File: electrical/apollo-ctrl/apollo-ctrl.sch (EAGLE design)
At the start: 62 parts, among them Q1 N-chan, Q2 N-chan, U1 NANO, U2 HONEYWELL-MPR, X1 BARREL-JACK, X2 SENSOR-O2

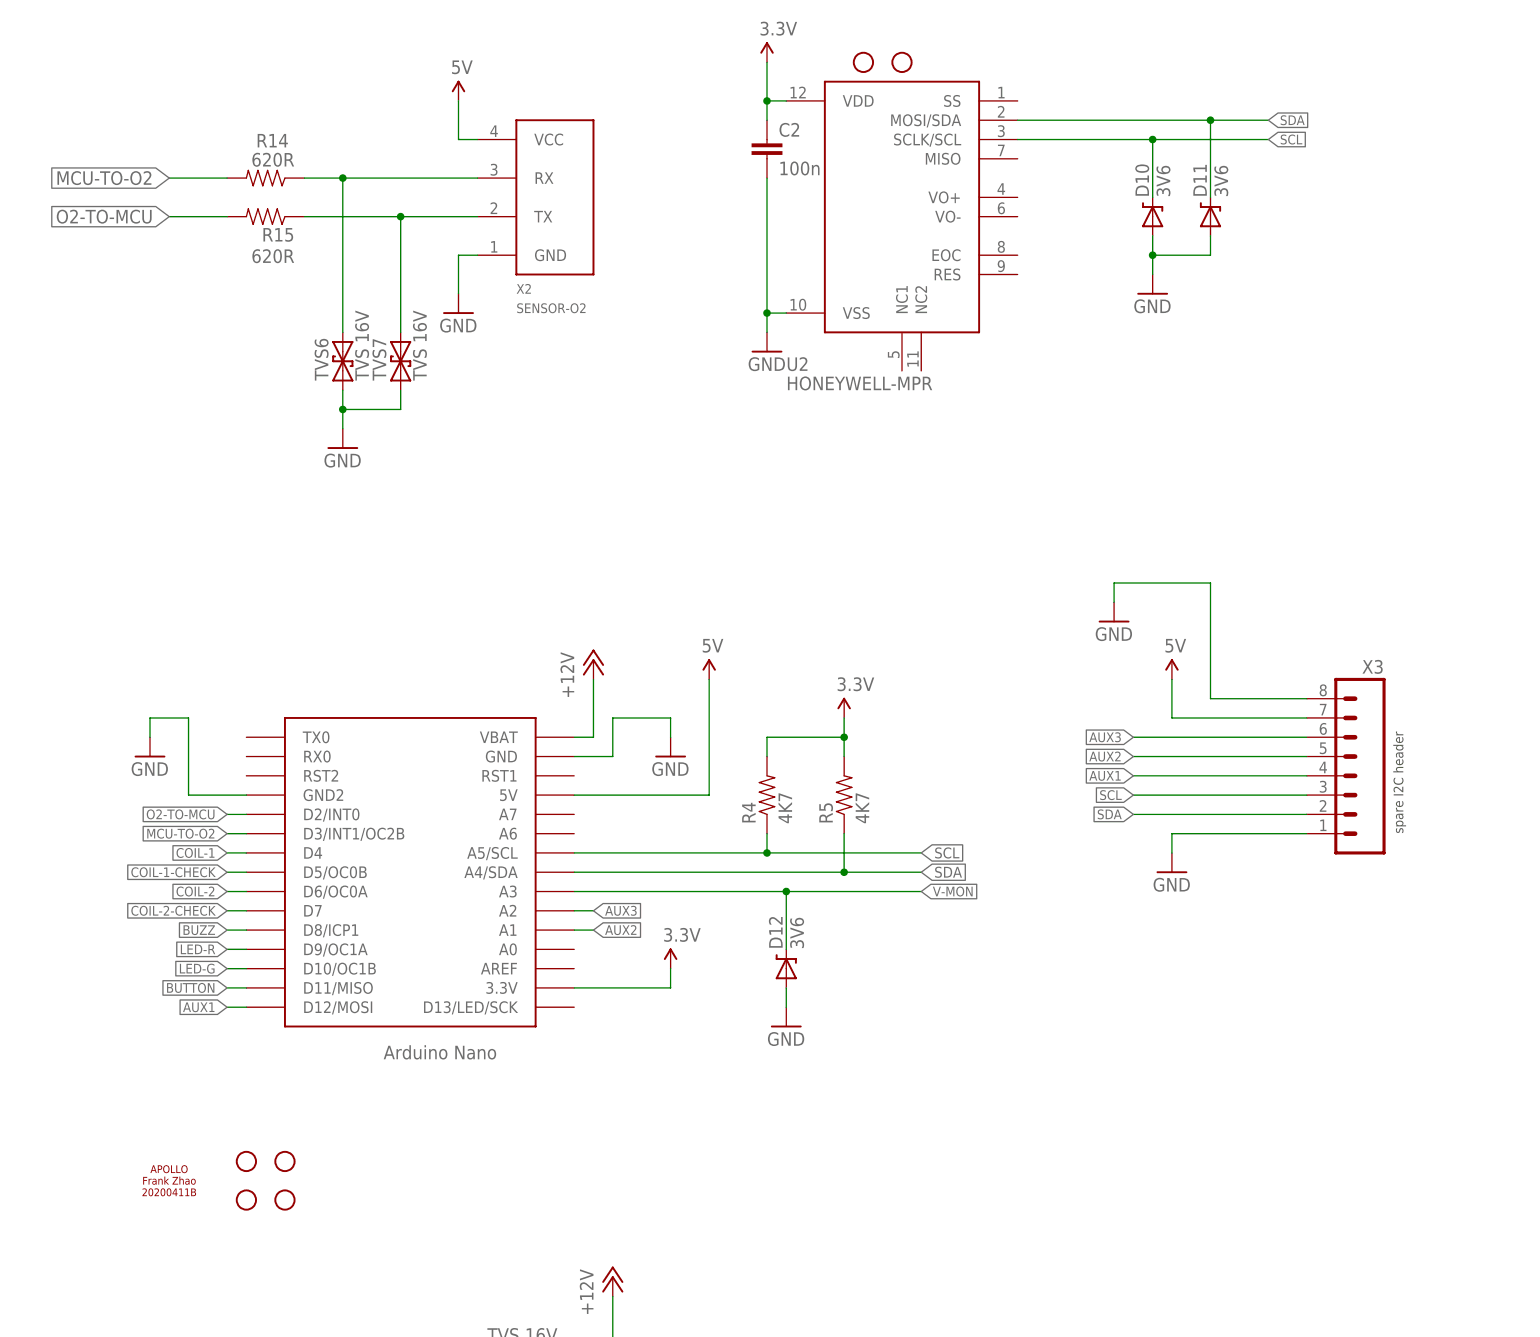
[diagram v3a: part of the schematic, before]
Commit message: changed to use Adafruit MPRLS
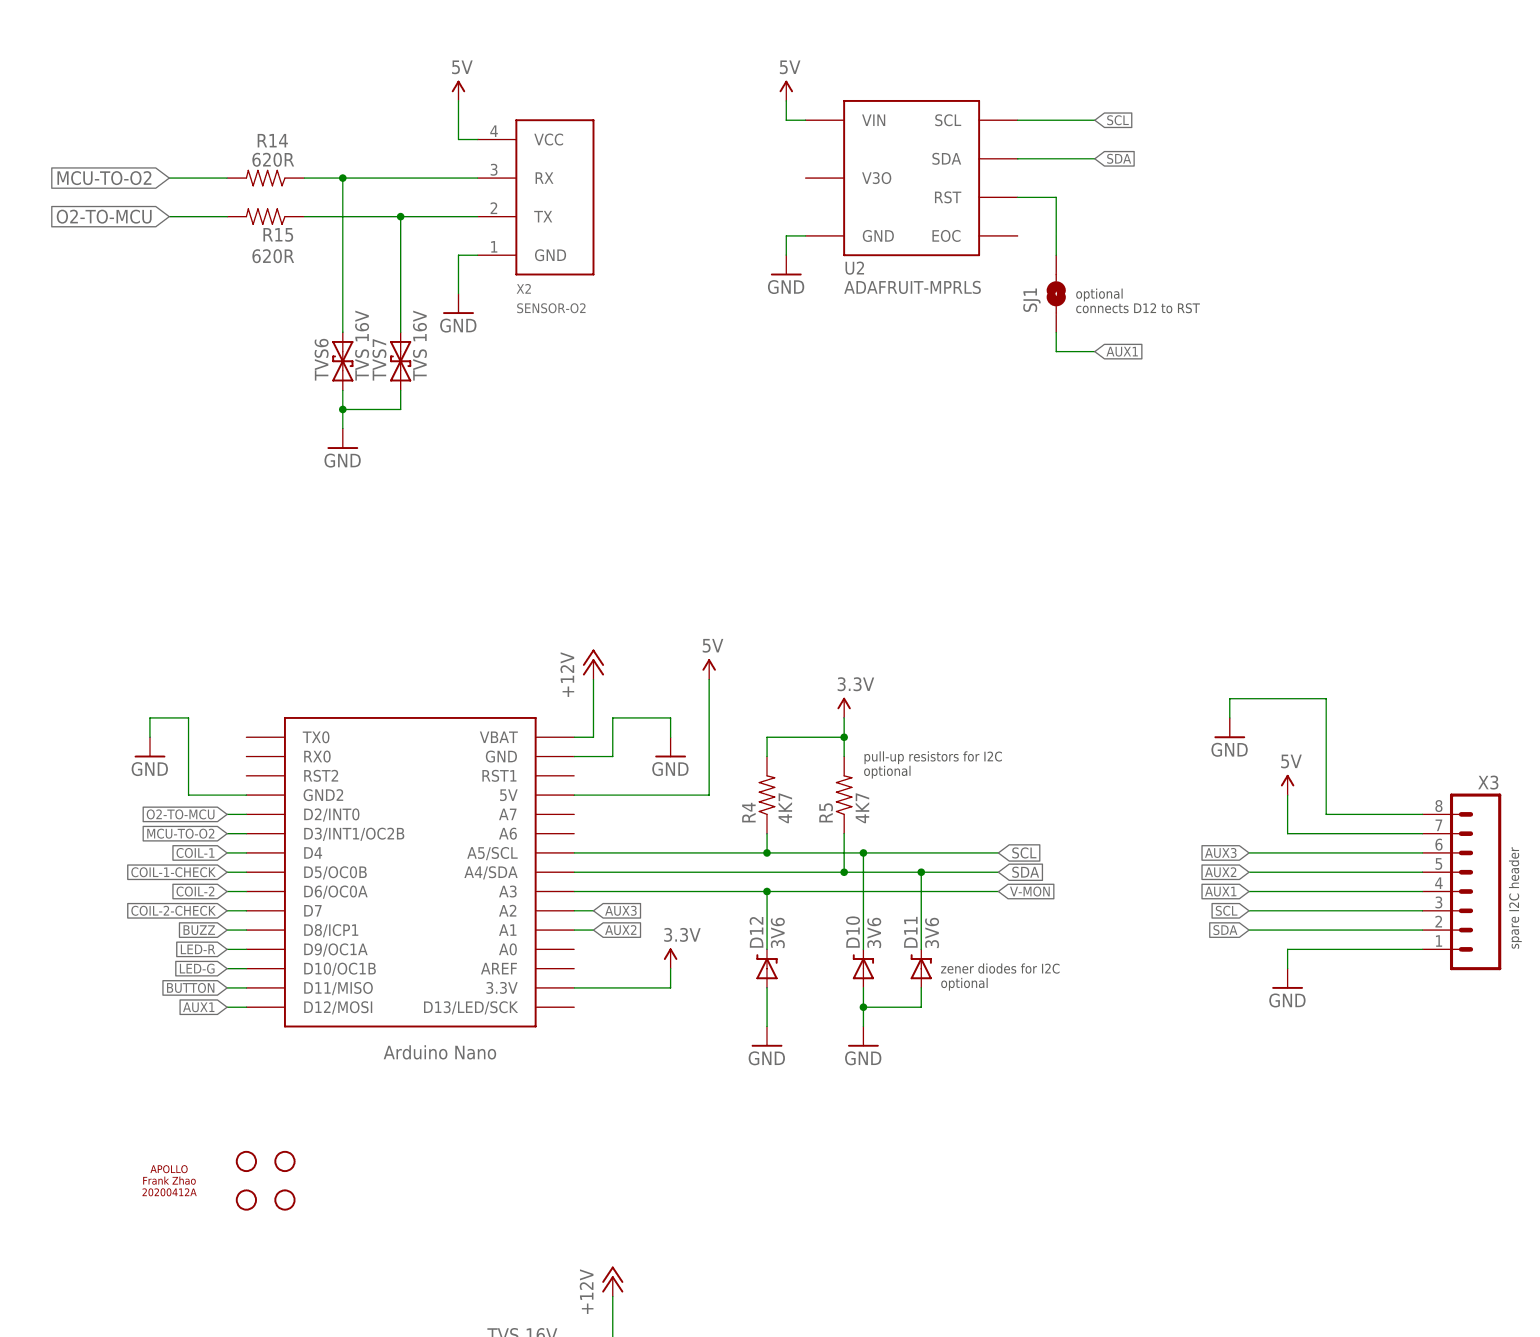
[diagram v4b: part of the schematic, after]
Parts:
- removed C2: 100n, apollo-ctrl:CAPPTH
- removed JP7, JP8: STAND-OFF, apollo-ctrl:STAND-OFF
- added SJ1: SOLDERJUMPERNO, apollo-ctrl:SOLDERJUMPERNO
- U2: value HONEYWELL-MPR -> ADAFRUIT-MPRLS; device apollo-ctrl:HONEYWELL-MPR-GAGE-DIY -> apollo-ctrl:ADAFRUIT-MPRLS-W-HOLES
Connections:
- new net N$1: SJ1.2, U2.RST
- net 3.3V: no longer C2.1, U2.VDD
- net 5V: now also U2.VIN
- net AUX1: now also SJ1.1
- net GND: now also U2.GND; no longer C2.2, U2.VSS
- net SCL: now also U2.SCL; no longer U2.SCLK/SCL
- net SDA: now also U2.SDA; no longer U2.MOSI/SDA
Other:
- note added: "optional connects D12 to RST"
- note added: "pull-up resistors for I2C optional"
- note added: "zener diodes for I2C optional"
- moved on the sheet: D10, D11, D12, X3

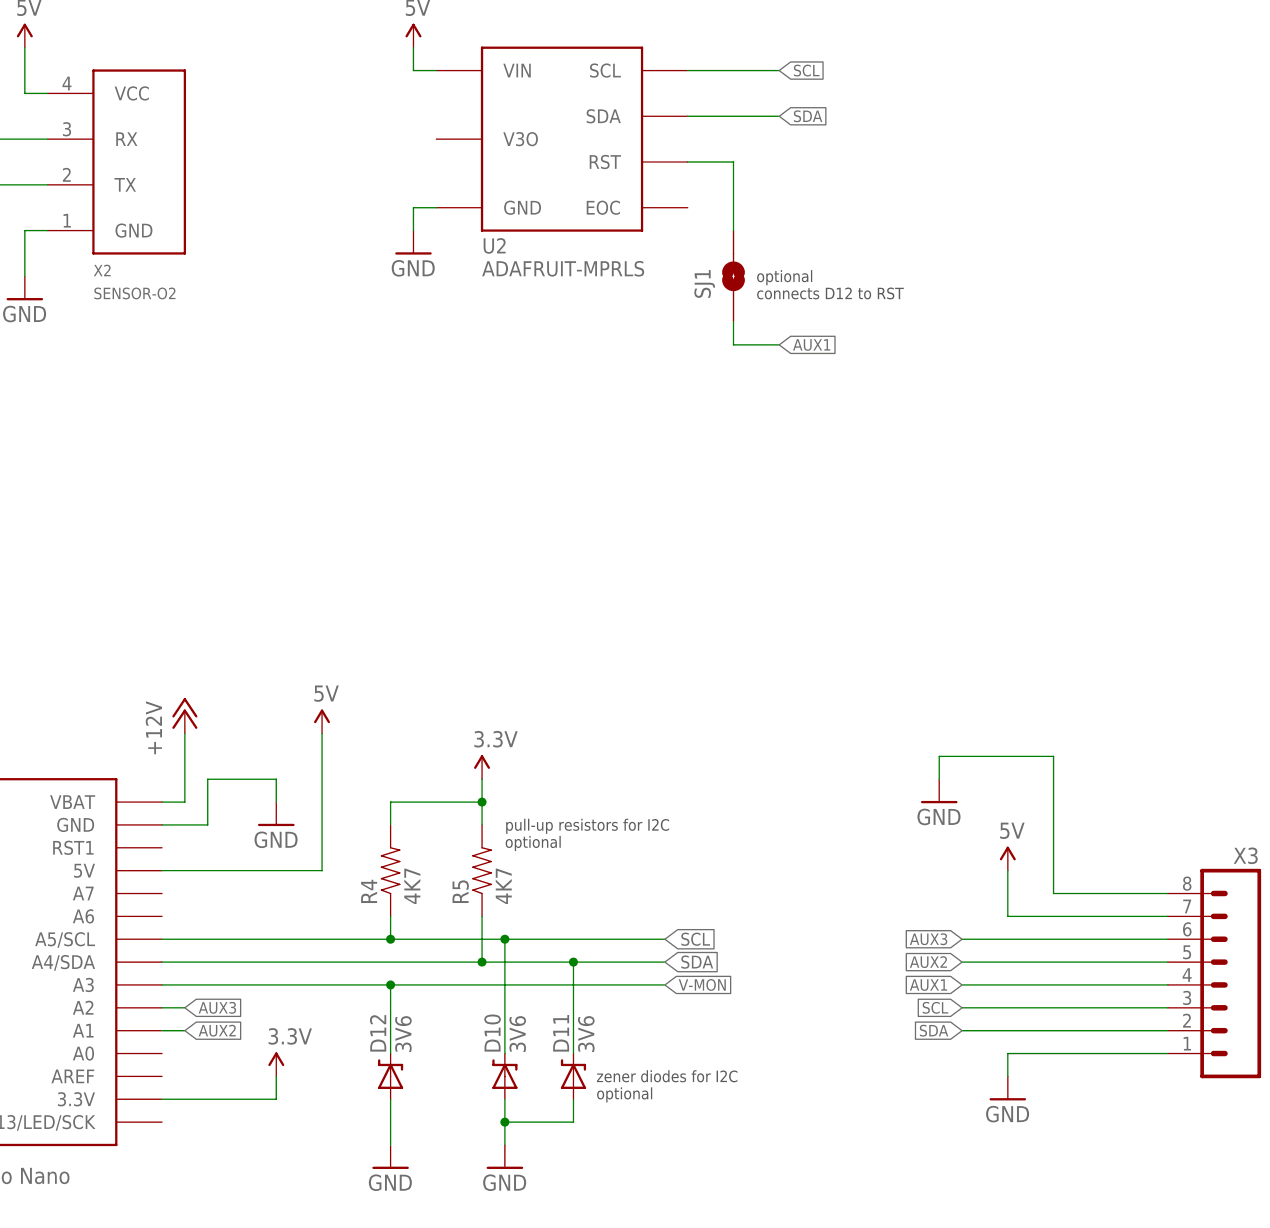
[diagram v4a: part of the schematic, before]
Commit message: added EOC signal to A0
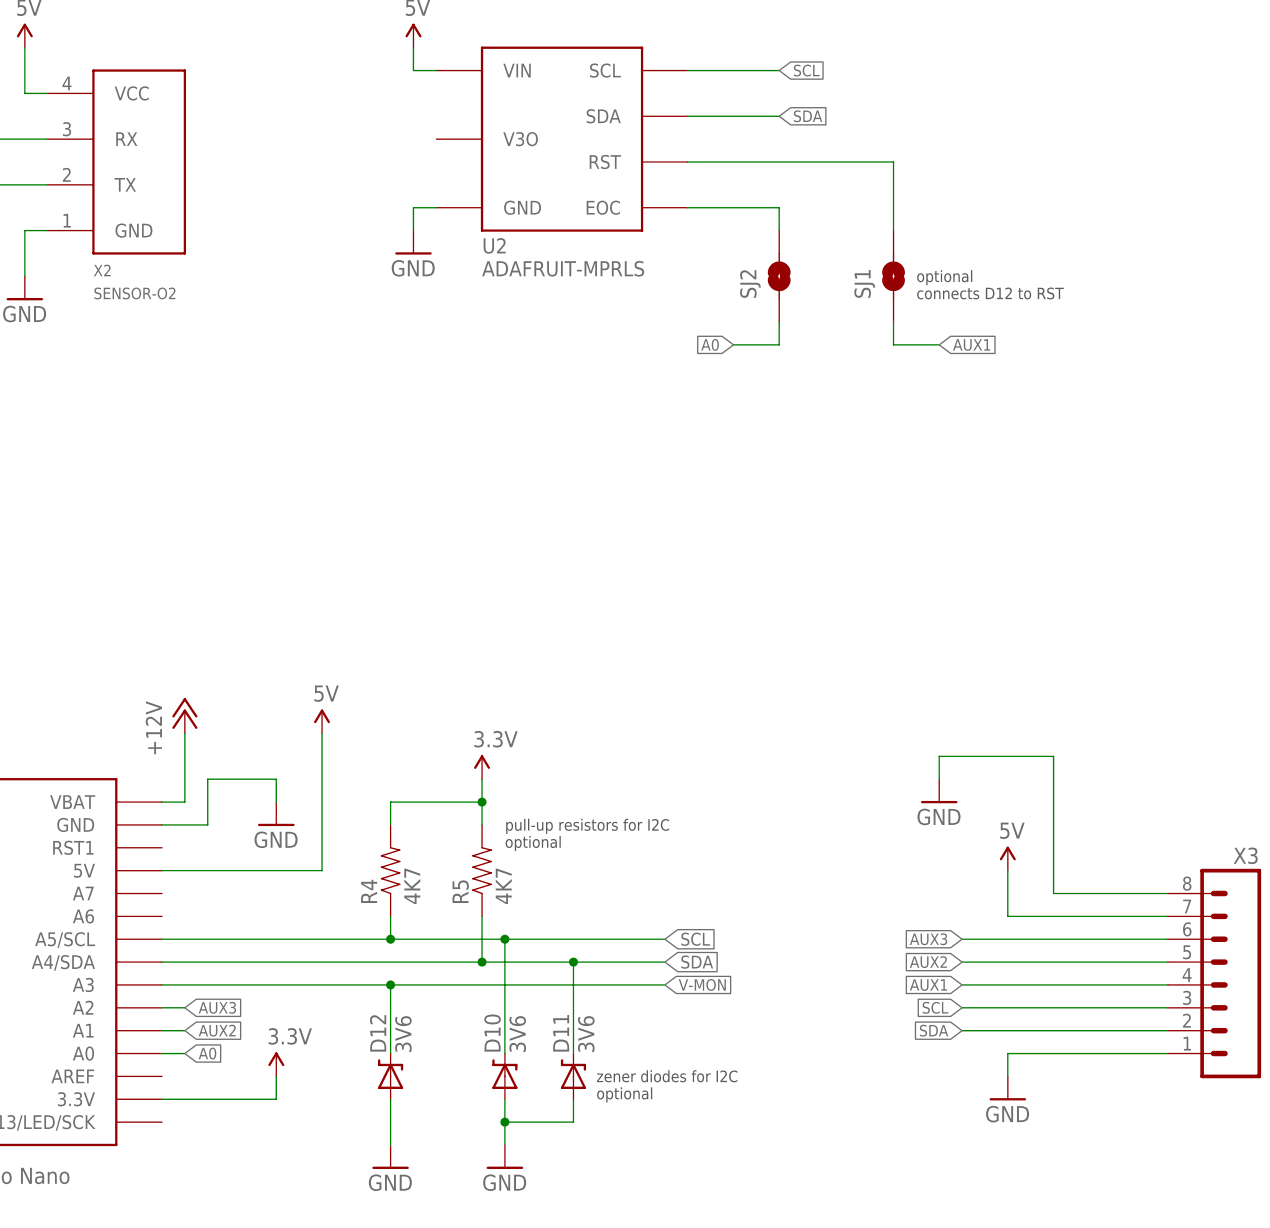
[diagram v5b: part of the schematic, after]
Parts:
- added SJ2: SOLDERJUMPERNO, apollo-ctrl:SOLDERJUMPERNO
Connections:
- new net A0: SJ2.1, U1.A0
- new net N$20: SJ2.2, U2.EOC
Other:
- moved on the sheet: SJ1
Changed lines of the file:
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@@
 <part name="P+9" library="apollo-ctrl" deviceset="5V" device=""/>
 <part name="SJ1" library="apollo-ctrl" deviceset="SOLDERJUMPER" device="NO" value=""/>
+<part name="SJ2" library="apollo-ctrl" deviceset="SOLDERJUMPER" device="NO" value=""/>
 </parts>
 <sheets>
@@
 <text x="91.44" y="53.34" size="1.27" layer="97">pull-up resistors for I2C
 optional</text>
-<text x="119.38" y="114.3" size="1.27" layer="97">optional
+<text x="137.16" y="114.3" size="1.27" layer="97">optional
 connects D12 to RST</text>
 </plain>
@@
 <attribute name="VALUE" x="80.264" y="145.796" size="1.778" layer="96"/>
 </instance>
-<instance part="SJ1" gate="1" x="116.84" y="116.84" rot="R90"/>
+<instance part="SJ1" gate="1" x="134.62" y="116.84" rot="R90"/>
+<instance part="SJ2" gate="1" x="121.92" y="116.84" rot="R90"/>
 </instances>
 <busses>
@@
 <segment>
 <pinref part="SJ1" gate="1" pin="1"/>
-<wire x1="116.84" y1="111.76" x2="116.84" y2="109.22" width="0.1524" layer="91"/>
-<wire x1="116.84" y1="109.22" x2="121.92" y2="109.22" width="0.1524" layer="91"/>
-<label x="121.92" y="109.22" size="1.27" layer="95" xref="yes"/>
+<wire x1="134.62" y1="111.76" x2="134.62" y2="109.22" width="0.1524" layer="91"/>
+<wire x1="134.62" y1="109.22" x2="139.7" y2="109.22" width="0.1524" layer="91"/>
+<label x="139.7" y="109.22" size="1.27" layer="95" xref="yes"/>
 </segment>
 </net>
@@
 <segment>
 <pinref part="U2" gate="G$1" pin="RST"/>
-<wire x1="111.76" y1="129.54" x2="116.84" y2="129.54" width="0.1524" layer="91"/>
+<wire x1="111.76" y1="129.54" x2="134.62" y2="129.54" width="0.1524" layer="91"/>
 <pinref part="SJ1" gate="1" pin="2"/>
-<wire x1="116.84" y1="129.54" x2="116.84" y2="121.92" width="0.1524" layer="91"/>
-</segment>
-</net>
+<wire x1="134.62" y1="129.54" x2="134.62" y2="121.92" width="0.1524" layer="91"/>
+</segment>
+</net>
+<net name="A0" class="0">
+<segment>
+<pinref part="U1" gate="G$1" pin="A0"/>
+<wire x1="53.34" y1="30.48" x2="55.88" y2="30.48" width="0.1524" layer="91"/>
+<label x="55.88" y="30.48" size="1.27" layer="95" xref="yes"/>
+</segment>
+<segment>
+<pinref part="SJ2" gate="1" pin="1"/>
+<wire x1="121.92" y1="111.76" x2="121.92" y2="109.22" width="0.1524" layer="91"/>
+<wire x1="121.92" y1="109.22" x2="116.84" y2="109.22" width="0.1524" layer="91"/>
+<label x="116.84" y="109.22" size="1.27" layer="95" rot="R180" xref="yes"/>
+</segment>
+</net>
+<net name="N$20" class="0">
+<segment>
+<pinref part="U2" gate="G$1" pin="EOC"/>
+<wire x1="111.76" y1="124.46" x2="121.92" y2="124.46" width="0.1524" layer="91"/>
+<pinref part="SJ2" gate="1" pin="2"/>
+<wire x1="121.92" y1="124.46" x2="121.92" y2="121.92" width="0.1524" layer="91"/>
+</segment>
+</net>
